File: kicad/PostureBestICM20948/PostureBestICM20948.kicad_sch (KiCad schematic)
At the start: 5 parts, among them U1 ICM-20948

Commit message: changes to rostik's design
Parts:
- added C3, C5: 0.1u, symbol Device:C
- added C4: 22u, symbol Device:C
- added J1: I2C/VDCG, symbol Connector:Conn_01x04_Socket
- added J2: INT1, symbol Connector:Conn_01x01_Socket
- added SW1: SW_SPDT, symbol Switch:SW_SPDT
- added U2: AMS1117-1.8, Package_TO_SOT_SMD:SOT-223-3_TabPin2, symbol Regulator_Linear:AMS1117-1.8
- C1: value 1u -> 22u
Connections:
- net GND: now also C1.2, C2.1, U1.18 (GND), U1.20 (GND), U1.9 (SDO/AD0), C3.1, C4.2, C5.1, J1.4 (Pin_4), U2.1 (GND); no longer C2.2
- net at R2.1: now also U1.24 (SDA/SDI), J1.2 (Pin_2)
- net at U1.23 (SCL/SCLK): now also R1.1, J1.3 (Pin_3); no longer R2.2
- net +3.3V: now reaches R1.2
- net +3.3V: now also C2.2, R2.2, U1.13 (VDD), U1.22 (~{CS}), C4.1, J1.1 (Pin_1), SW1.1 (A), U2.3 (VI); no longer U1.24 (SDA/SDI)
- net at U1.10 (REGOUT): now also C3.2
- new net: J2.1 (Pin_1), SW1.3 (C)
- new net +1V8: C1.1, C5.2, U1.8 (VDDIO), U2.2 (VO)
- new net INT1_OUT: SW1.2 (B), U1.12 (INT1)
- no-connect marks 0 -> 2
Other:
- note added: "By default, wake pin pulled up but by switching, the chip can be awakened via GPIO"
- note added: "I2C addr with SD0 tied low b1101000 / 0x68"
- note added: "IO Power"
- note added: "Order reconfigured to match output of I2C mux on motherboard without crossing jumper wires."
- company: (none) -> Capstone C6
- title: (none) -> IMU Module
- moved on the sheet: C2, R1, R2, U1

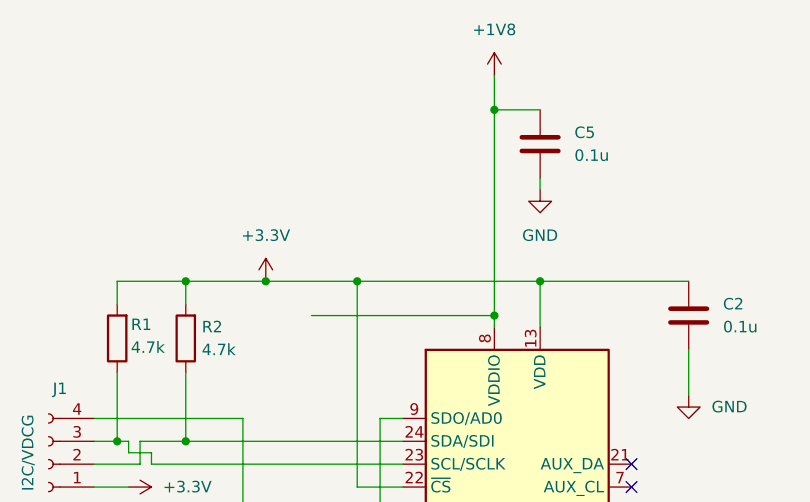
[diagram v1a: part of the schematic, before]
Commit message: ble and i2c mux example code in stm32cubeide/ble_testing
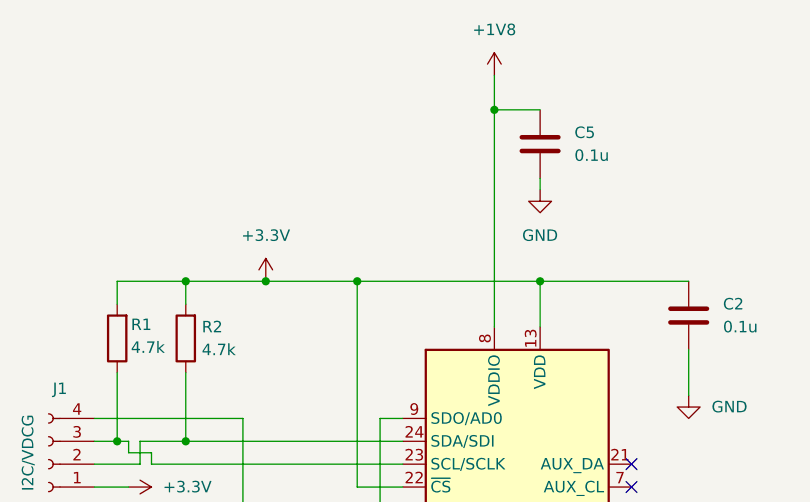
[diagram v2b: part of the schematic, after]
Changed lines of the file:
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@@
-	)
-	(junction
-		(at 111.76 55.88)
-		(diameter 0)
-		(color 0 0 0 0)
 	)
 	(junction
@@
 	(wire
 		(pts
-			(xy 111.76 33.02) (xy 111.76 55.88)
-		)
-		(stroke
-			(width 0)
-			(type default)
-		)
-	)
-	(wire
-		(pts
 			(xy 88.9 116.84) (xy 93.98 116.84)
 		)
@@
 	(wire
 		(pts
-			(xy 91.44 55.88) (xy 111.76 55.88)
-		)
-		(stroke
-			(width 0)
-			(type default)
-		)
-	)
-	(wire
-		(pts
-			(xy 111.76 55.88) (xy 111.76 57.15)
-		)
-		(stroke
+			(xy 111.76 33.02) (xy 111.76 57.15)
+		)
+		(stroke

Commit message: Revert "ble and i2c mux example code in stm32cubeide/ble_testing"
This reverts commit 00b30e45b3f9405408dd6880b6cf67d626e086a2.
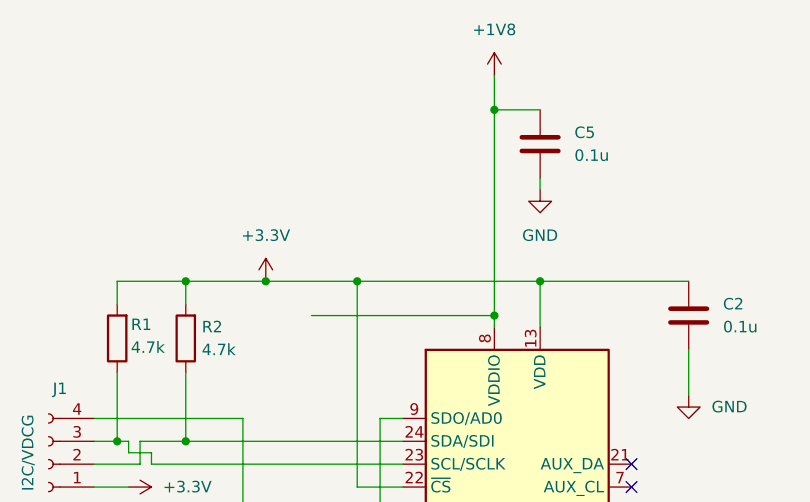
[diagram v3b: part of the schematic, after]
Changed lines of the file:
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@@
+	)
+	(junction
+		(at 111.76 55.88)
+		(diameter 0)
+		(color 0 0 0 0)
 	)
 	(junction
@@
 	(wire
 		(pts
+			(xy 111.76 33.02) (xy 111.76 55.88)
+		)
+		(stroke
+			(width 0)
+			(type default)
+		)
+	)
+	(wire
+		(pts
 			(xy 88.9 116.84) (xy 93.98 116.84)
 		)
@@
 	(wire
 		(pts
-			(xy 111.76 33.02) (xy 111.76 57.15)
-		)
-		(stroke
+			(xy 91.44 55.88) (xy 111.76 55.88)
+		)
+		(stroke
+			(width 0)
+			(type default)
+		)
+	)
+	(wire
+		(pts
+			(xy 111.76 55.88) (xy 111.76 57.15)
+		)
+		(stroke

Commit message: IMU PCB design 1
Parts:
- removed J2: INT1, symbol Connector:Conn_01x01_Socket
- C1, C2, C3, C5: footprint (none) -> Capacitor_SMD:C_0402_1005Metric
- C4: value 22u -> 10u; footprint (none) -> Capacitor_SMD:C_0402_1005Metric
- J1: footprint (none) -> Connector_PinSocket_2.54mm:PinSocket_1x04_P2.54mm_Horizontal
- R1, R2: footprint (none) -> Resistor_SMD:R_0603_1608Metric
- SW1: footprint (none) -> external_footprints:SW_SSSS811101
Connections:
- net GND: now also SW1.3 (C)
